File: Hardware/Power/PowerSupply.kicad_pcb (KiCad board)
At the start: 4 copper layers, 172 x 85 mm, 206 parts, among them Q1 PSMN1R5-25MLHX, Q10 BSS84, Q11 2N7002PW, Q12 2N7002PW, Q13 2N7002PW, Q14 Si7141DP, Q15 BSS84, Q16 Si7141DP, Q17 Si7141DP, Q18 Si7141DP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

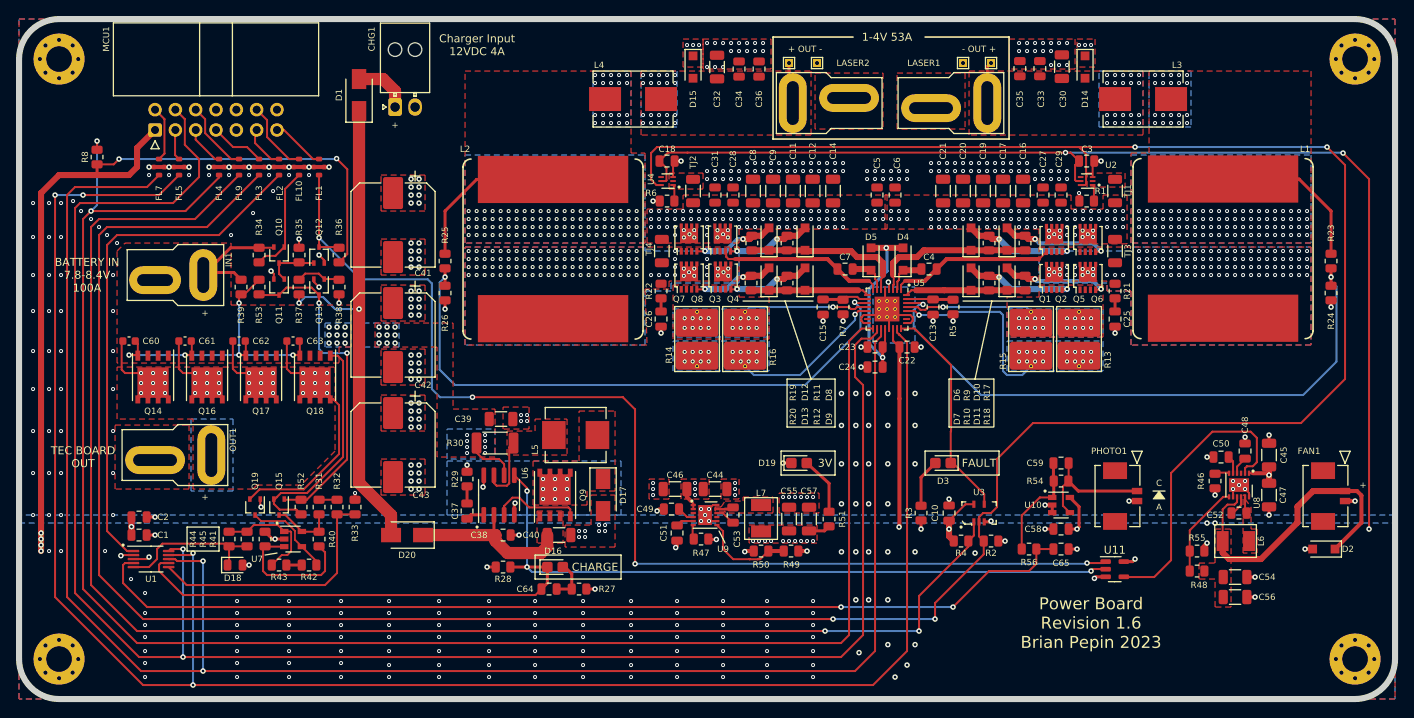
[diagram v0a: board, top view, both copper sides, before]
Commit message: recover v1 of driver board
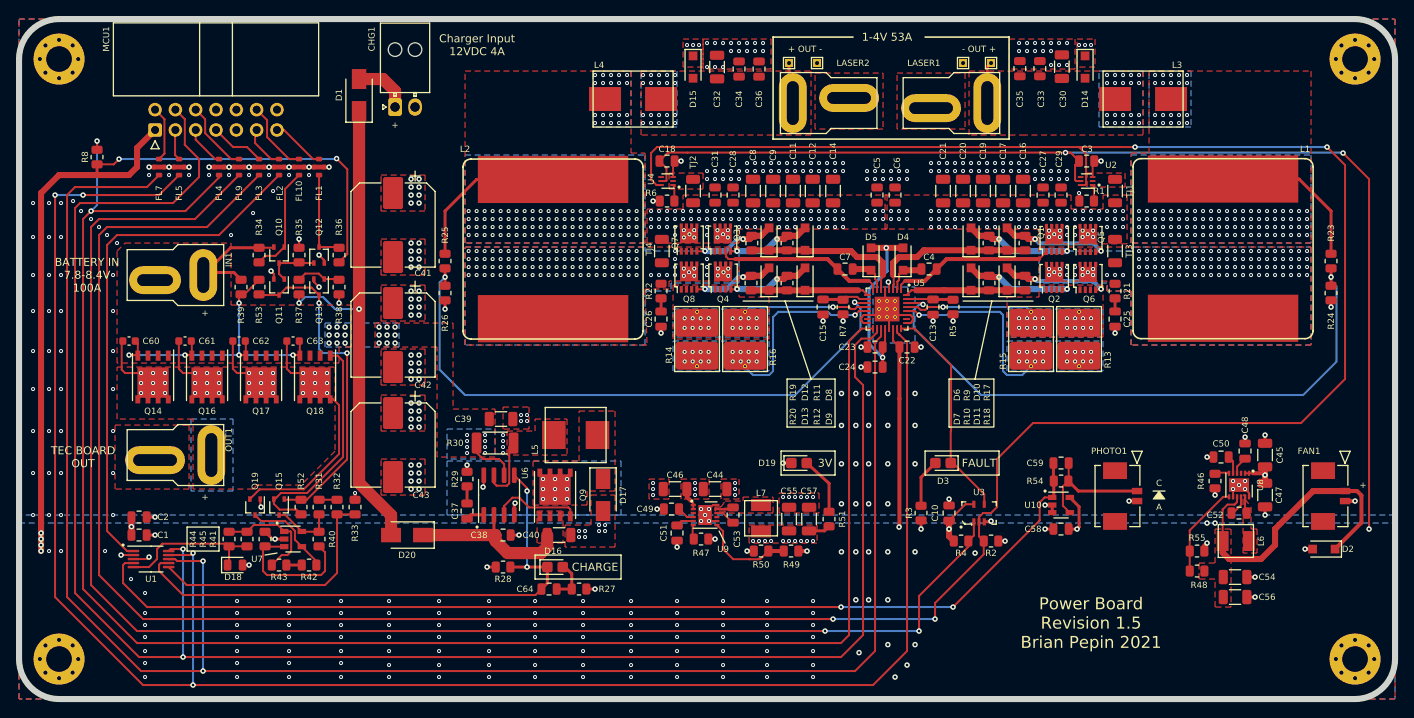
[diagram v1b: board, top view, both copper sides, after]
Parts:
- removed C65: 10uF, Capacitor_SMD:C_0805_2012Metric
- removed R56: 51k, Resistor_SMD:R_0805_2012Metric
- removed U11: 74AHC1G00, Package_TO_SOT_SMD:SOT-23-5
- C58: value 10uF -> .1uF
- moved C45 0.50 mm to (205.8, 119.5)
- moved C47 0.50 mm to (205.8, 124.5)
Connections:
- C59 pad 1: Net-(C59-Pad1) -> LASER_MON
- H1 pad 1: unconnected-(H1-Pad1) -> Net-(H1-Pad1)
- H2 pad 1: unconnected-(H2-Pad1) -> Net-(H2-Pad1)
- H3 pad 1: unconnected-(H3-Pad1) -> Net-(H3-Pad1)
- H4 pad 1: unconnected-(H4-Pad1) -> Net-(H4-Pad1)
- MCU1 pad 10: unconnected-(MCU1-Pad10) -> /TEC_ENABLE
- MCU1 pad 8: unconnected-(MCU1-Pad8) -> /CS_TEC_SET
- MCU1 pad 9: unconnected-(MCU1-Pad9) -> /CS_TEC_READ
- R54 pad 1: Net-(C59-Pad1) -> LASER_MON
- U10 pad 1: Net-(C59-Pad1) -> LASER_MON
- U2 pad 4: unconnected-(U2-Pad4) -> Net-(U2-Pad4)
- U4 pad 4: unconnected-(U4-Pad4) -> Net-(U4-Pad4)
- U5 pad 15: unconnected-(U5-Pad15) -> Net-(U5-Pad15)
- U5 pad 26: unconnected-(U5-Pad26) -> Net-(U5-Pad26)
- U8 pad 2: Net-(U11-Pad4) -> VDC
- U8 pad 3: unconnected-(U8-Pad3) -> Net-(U8-Pad3)
- U9 pad 3: unconnected-(U9-Pad3) -> Net-(U9-Pad3)
- U9 pad 9: unconnected-(U9-Pad9) -> Net-(U9-Pad9)
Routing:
- net ~{INTERLOCK_EN}: track 146.0 -> 11.5 mm, vias 4 -> 0
- net ~{CHARGE}: track 144.0 -> 71.3 mm, vias 3 -> 2
- net Net-(U11-Pad4): track 36.3 -> 0.00 mm
- net Net-(C59-Pad1): track 13.3 -> 0.00 mm
- net LASER_MON: track 125.3 -> 132.4 mm
- net +3V3: track 303.2 -> 301.6 mm, vias 30 -> 29
- net /LaserDriver/OUT2: track 75.7 -> 76.7 mm
- net +BATT: track 52.3 -> 52.9 mm
- net GND: vias 457 -> 455
- net VDC: vias 238 -> 242
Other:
- board text added: "Power Board Revision 1.5 Brian Pepin 2021"
- board text removed: "Power Board Revision 1.6 Brian Pepin 2023"
